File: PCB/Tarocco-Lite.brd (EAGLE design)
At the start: 46.4 x 27.9 mm, 32 parts, among them IC1 CY8C4545PVI, U1 DRV8801PWP

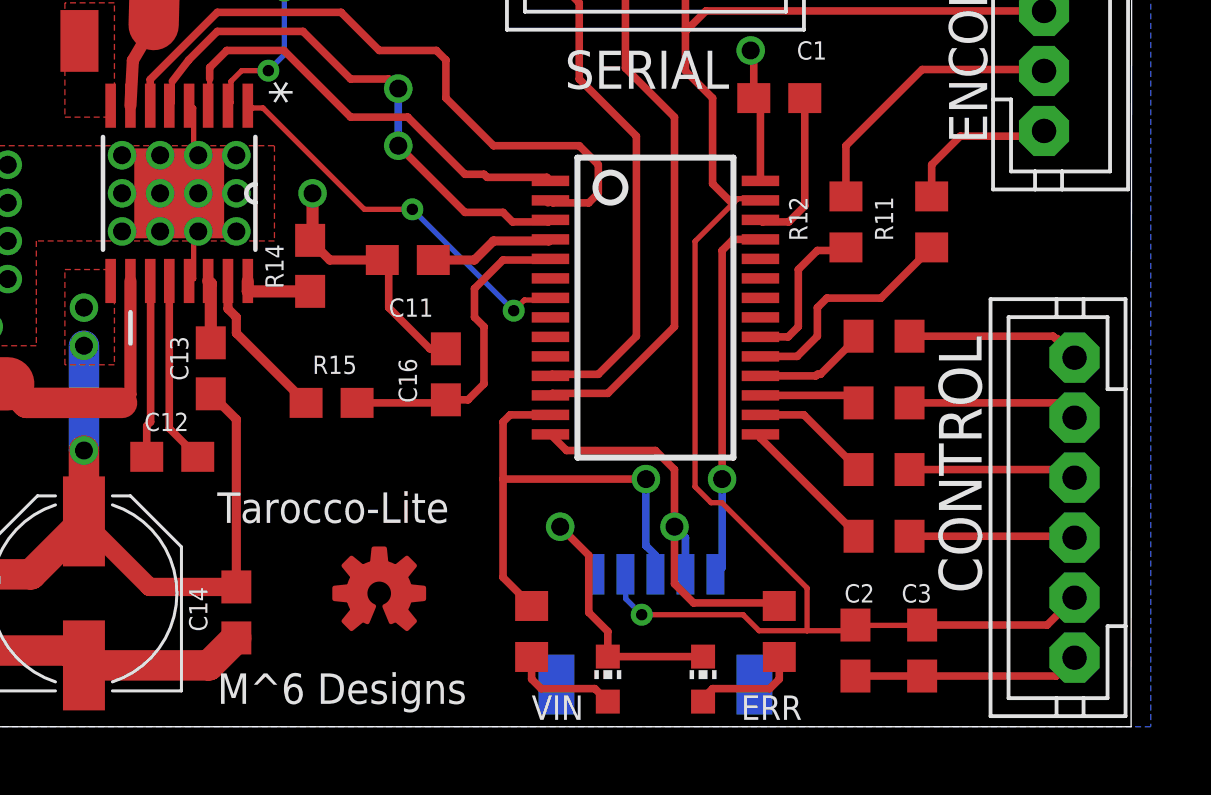
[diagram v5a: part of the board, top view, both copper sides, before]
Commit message: SMD cap swap
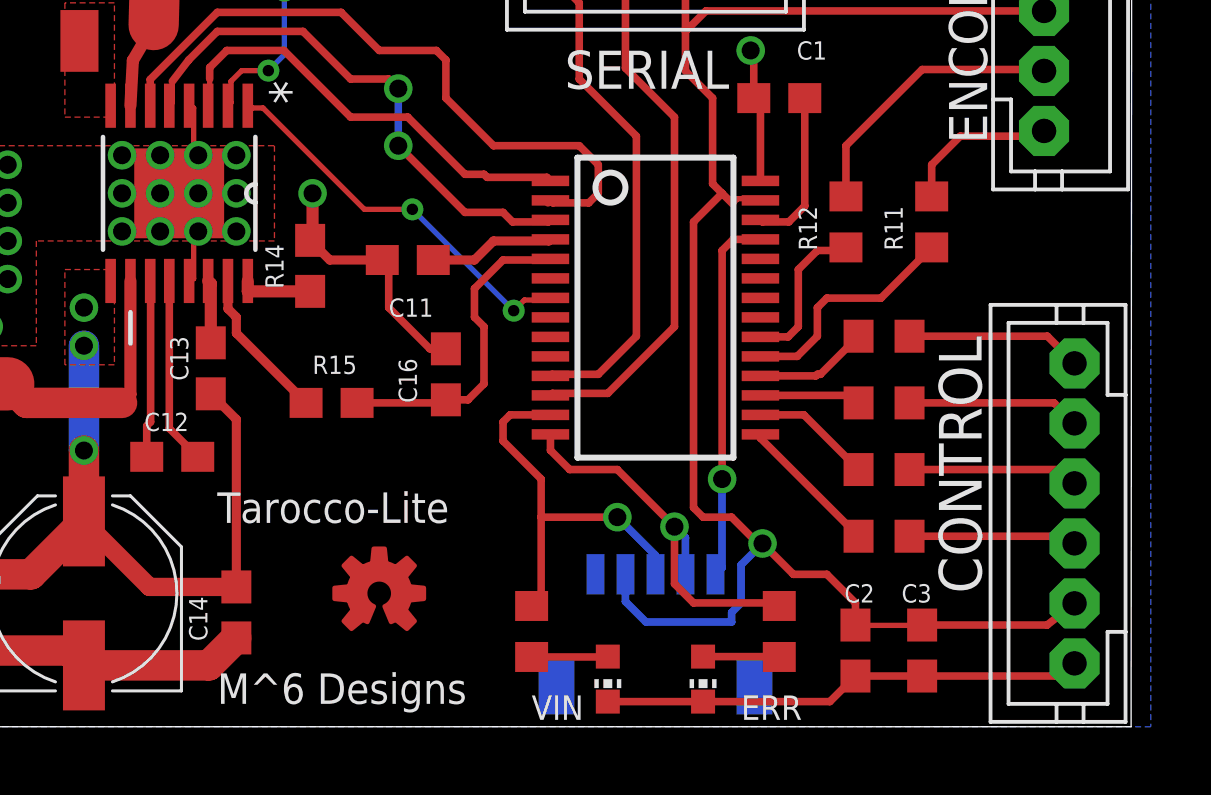
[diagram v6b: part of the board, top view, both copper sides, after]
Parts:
- moved CONTROL 0.19 mm to (54.6, 7.11)
- turned ERR to 180 degrees
- turned VIN to 180 degrees
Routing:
- net SWDIO: track 16.3 -> 13.9 mm
- net 5V: track 68.7 -> 69.9 mm
- net N$24: track 3.66 -> 2.55 mm
- net N$25: track 3.59 -> 2.55 mm
- net N$14: track 6.70 -> 5.88 mm
- net SWDCLK: track 14.0 -> 13.2 mm
- net GND: track 51.6 -> 51.9 mm, vias 27 -> 26

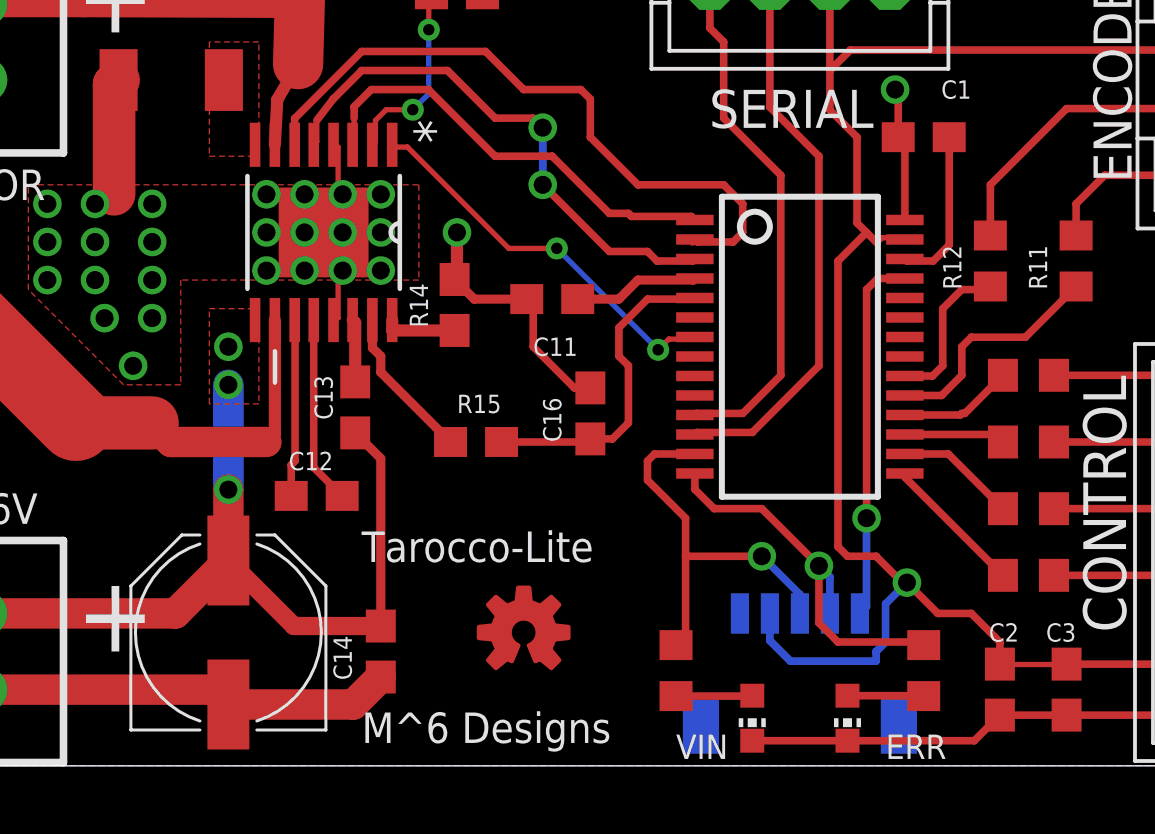
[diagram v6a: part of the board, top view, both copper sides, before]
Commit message: Moved bootloader location for functionality added proper BOM
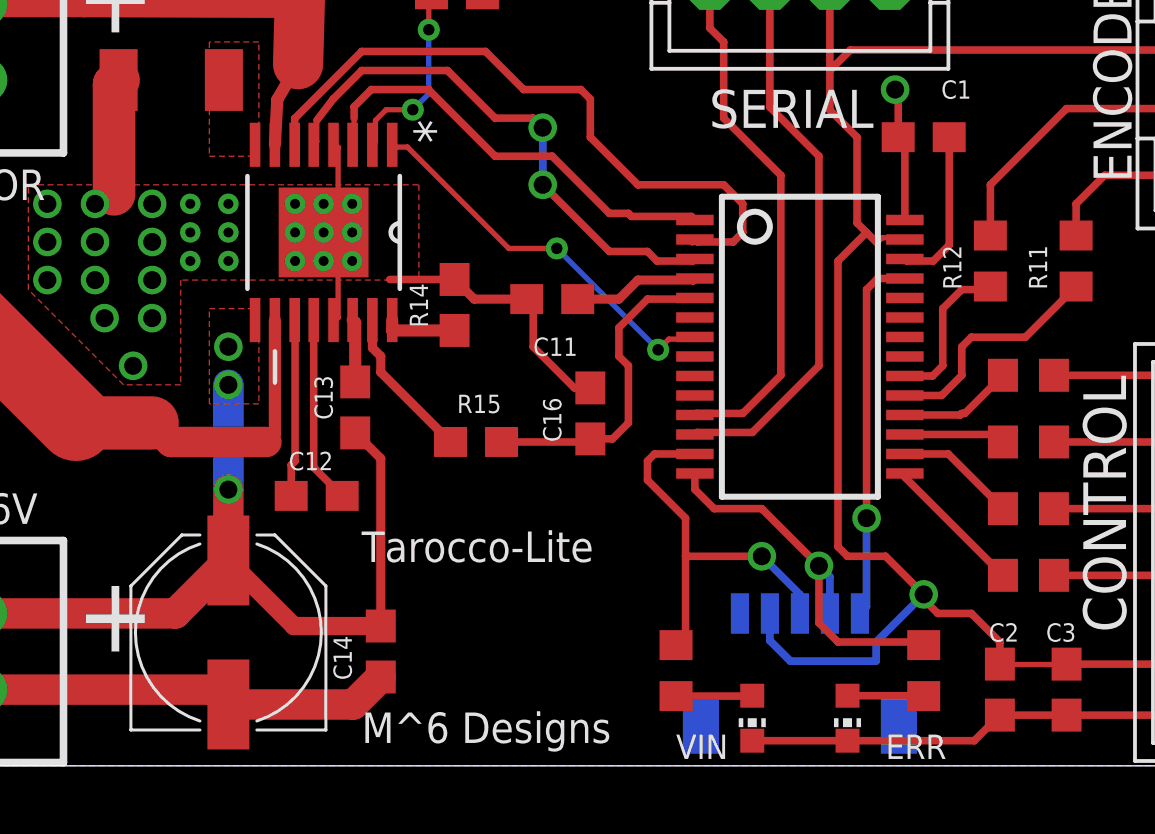
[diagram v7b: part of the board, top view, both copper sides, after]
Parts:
- removed U$1: (no value), SparkFun-Aesthetics:OSHW-LOGO-S_COPPER
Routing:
- net GND: track 51.9 -> 52.6 mm, vias 26 -> 28

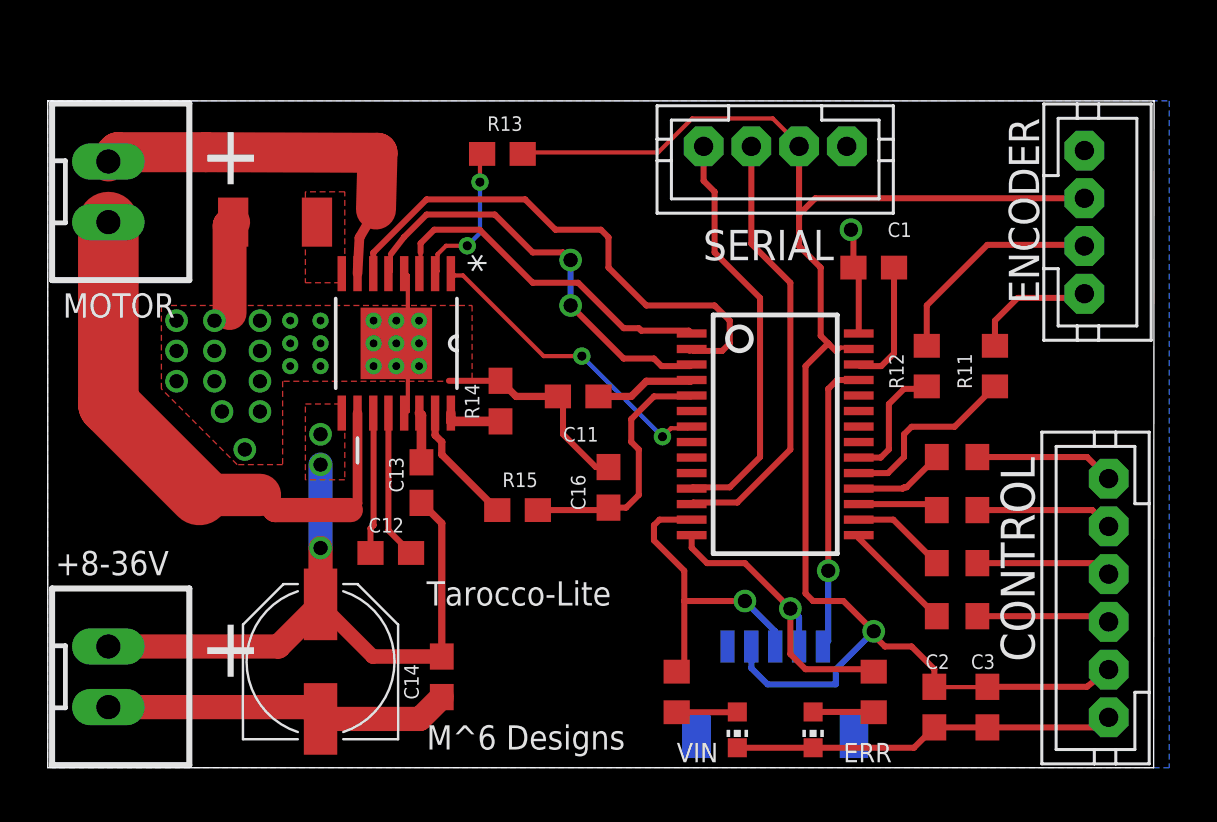
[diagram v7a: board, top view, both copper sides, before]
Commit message: ground pour
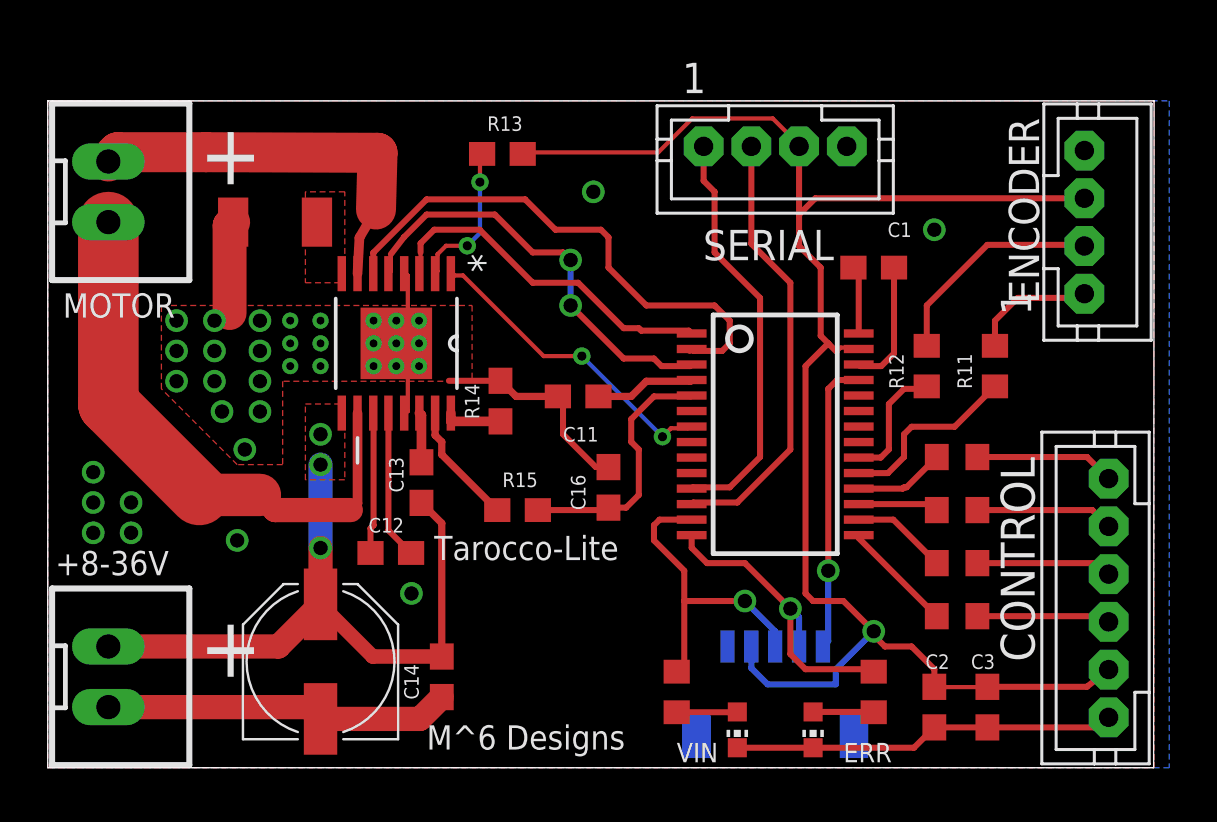
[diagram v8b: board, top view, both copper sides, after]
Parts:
- added U$1: (no value), SparkFun-Aesthetics:OSHW-LOGO-L_COPPER
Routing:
- net GND: track 52.6 -> 50.9 mm, vias 28 -> 36
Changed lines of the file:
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@@
 <text x="16.51" y="25.7175" size="2.54" layer="25" align="center-left">+</text>
 <text x="26.035" y="1.27" size="1.016" layer="25" align="center-left">M^6 Designs</text>
-<text x="26.035" y="7.3025" size="1.016" layer="25" ratio="16" align="center-left">Tarocco-Lite</text>
+<text x="26.3525" y="9.2075" size="1.016" layer="25" ratio="16" align="center-left">Tarocco-Lite</text>
 <text x="25.0825" y="10.16" size="0.6096" layer="25" rot="R180" align="center-left">C12</text>
 <text x="24.765" y="13.0175" size="0.6096" layer="25" rot="R270" align="center-left">C13</text>
@@
 <vertex x="27.6225" y="15.24"/>
 <vertex x="21.59" y="15.24"/>
+</polygon>
+<polygon width="0.254" layer="30">
+<vertex x="19.05" y="16.51"/>
+<vertex x="19.05" y="13.335"/>
+<vertex x="18.415" y="13.335"/>
+<vertex x="15.24" y="16.51"/>
 </polygon>
 </plain>
@@
 <attribute name="VALUE" x="37.1475" y="2.2225" size="1.27" layer="27" rot="R270"/>
 </element>
+<element name="U$1" library="SparkFun-Aesthetics" package="OSHW-LOGO-L_COPPER" value="" x="31.4325" y="4.7625"/>
 </elements>
 <signals>
@@
 <wire x1="53.9975" y1="1.69" x2="54.61" y2="2.112" width="0.254" layer="1"/>
 <wire x1="44.14" y1="18.195" x2="44.14" y2="20.7325" width="0.254" layer="1"/>
-<wire x1="44.14" y1="20.7325" x2="43.9175" y2="20.955" width="0.254" layer="1"/>
-<wire x1="43.9175" y1="20.955" x2="43.9175" y2="22.44" width="0.254" layer="1"/>
-<wire x1="43.9175" y1="22.44" x2="43.815" y2="22.5425" width="0.254" layer="1"/>
-<via x="43.815" y="22.5425" extent="1-16" drill="0.6"/>
+<wire x1="43.9175" y1="20.955" x2="44.14" y2="20.7325" width="0.254" layer="1"/>
 <wire x1="39.0525" y1="0.8375" x2="42.2275" y2="0.8375" width="0.254" layer="1"/>
 <wire x1="42.2275" y1="0.8375" x2="46.455" y2="0.8375" width="0.254" layer="1"/>
@@
 <via x="20.32" y="17.78" extent="1-16" drill="0.3302"/>
 <via x="20.32" y="16.8275" extent="1-16" drill="0.3302"/>
+<polygon width="0.4064" layer="1" rank="6">
+<vertex x="10.16" y="27.94"/>
+<vertex x="10.16" y="0"/>
+<vertex x="56.515" y="0"/>
+<vertex x="56.515" y="0.3175"/>
+<vertex x="56.515" y="27.94"/>
+</polygon>
+<via x="47.3075" y="22.5425" extent="1-16" drill="0.6"/>
+<via x="12.065" y="12.3825" extent="1-16" drill="0.6"/>
+<via x="12.065" y="11.1125" extent="1-16" drill="0.6"/>
+<via x="12.065" y="9.8425" extent="1-16" drill="0.6"/>
+<via x="13.6525" y="9.8425" extent="1-16" drill="0.6"/>
+<via x="13.6525" y="11.1125" extent="1-16" drill="0.6"/>
+<via x="18.0975" y="9.525" extent="1-16" drill="0.6"/>
+<via x="33.02" y="24.13" extent="1-16" drill="0.6"/>
+<via x="25.4" y="7.3025" extent="1-16" drill="0.6"/>
 </signal>
 <signal name="5V">
